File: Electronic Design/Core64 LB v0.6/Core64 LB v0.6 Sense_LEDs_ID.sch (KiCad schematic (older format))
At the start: 25 parts, among them J10 TSM-106-03-T-DV‎, J11 HEADER_8-PIN_0.1, J17 LED Cur. Mon., U1 74HC02, U3 LM393, U3 SN74LV1T125DBVR, U4 M24C02-RMN, U7 LM393

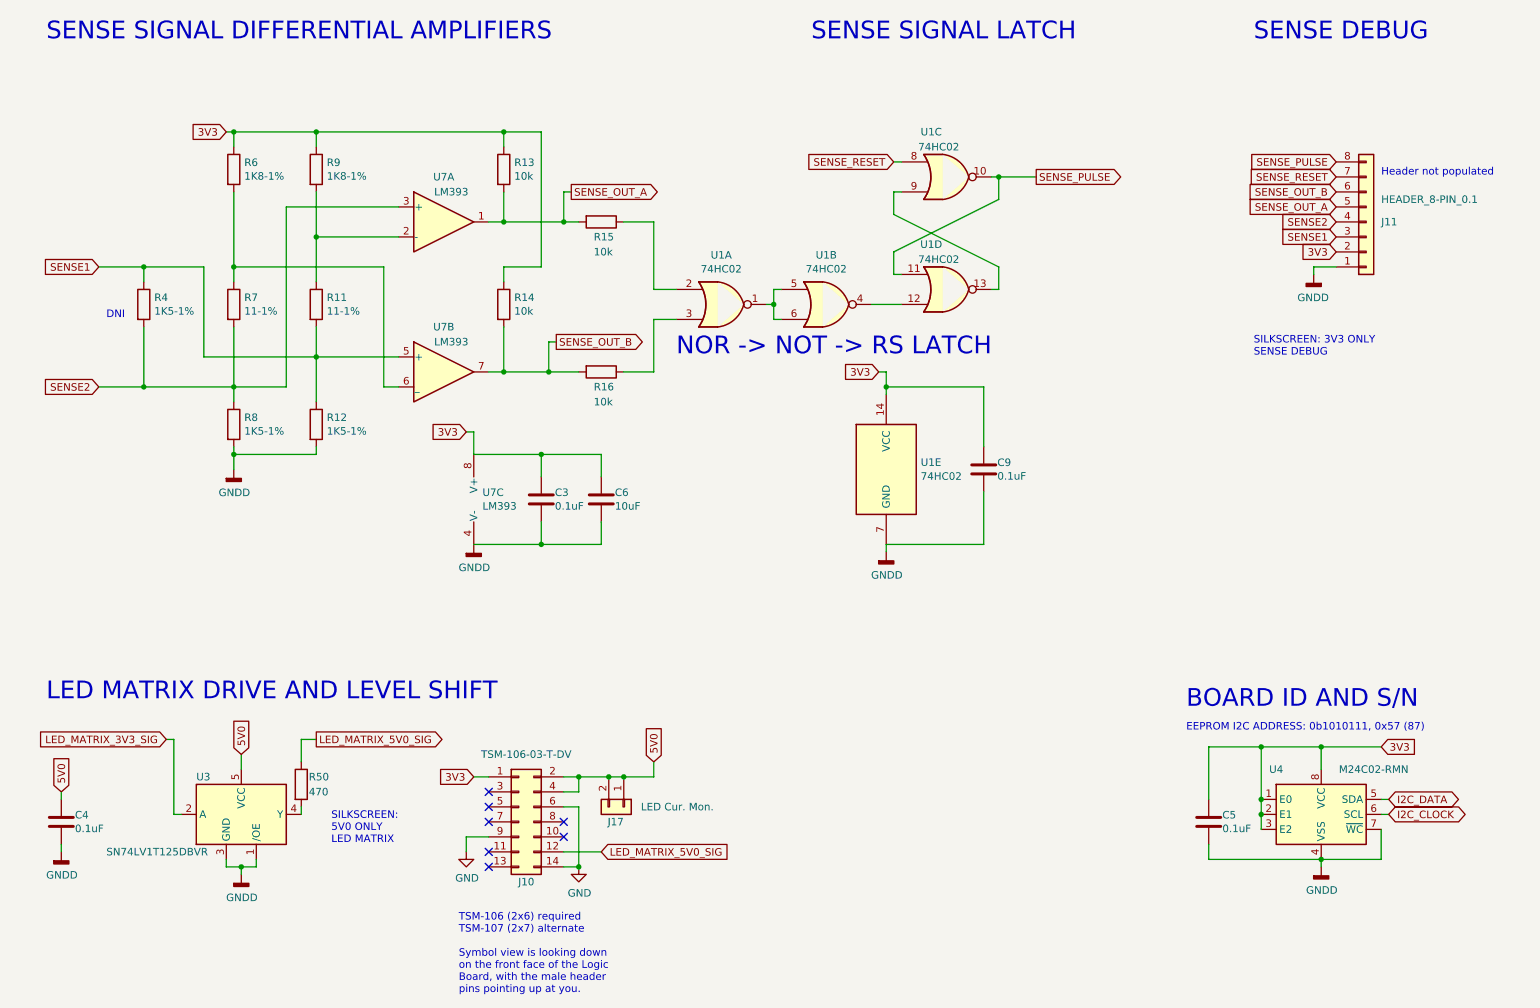
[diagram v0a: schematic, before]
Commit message: APPLY LOGIC BOARD V0.5 FIXES NEEDED TO BE V0.6 U1 silk screen should be placed by pin 1 not pin 7 Check J1 and J2 labels so J1 is on the left, like it is for the Core Board Remove Header for old LED Matrix, since is no longer needed and it is in the way. RTC Notes on schematic, must add THREE things, typo change from TWO. Below JP5 Teensy Charge Enable is a rogue "+" on the silk screen Left of R56 is a dead-end trace stub. Doesn't hurt anything but it's not right. 6.8 Ohm Core Current Limit Resistors can move to 5%. JP1/2 for OLED should be JP1/2 on the OLED silk screen, not JP3/4 Silk screen, left header row, swap SEN1 and SEN2 text so they match to S1 and S2 correctly on the inner perimeter. Move to larger logo and other text on the backside Update silk screen for all boards with P/Ns, bare board. Move top row of TFT LCD support down 0.55mm. Add 470 resistor to gate of core array enable to limit current. Change I2C pull-up resistors from 2.2K to 1.2K 20% (E12 series is most common, and values overlap) Remove two dead-end GND (BAT-) traces between/below Teensy 25/26, and over to QWIIC. Add I2C series resistors 68 Ohm at output of Teensy. Move the 470uF LED 5V0 capacitor, down to be between 5V0 Cur Mon and Teensy Charge enable jumpers, out of the way of the batteries. New stylus position is on left, so the 3V3 capacitor needs to move in a few mm to allow it to pass through. Provide thru-holes for alternate 3.3V and 5V bulk capacitor options. Propagation through sense logic chips was 200ns, reduce PU to 1K2 and remove inline 10Ks. Now 50ns. Voltage divider and other resistors, consolidated to 10K resistors. Keep the two 10K resistors on the 5V0 MON. Add a SJ in series to isolate from Hall Switches. Replace the inline 10K resistors in the all optional Voltage Monitoring lines with closed SJs instead. Clean-up all the horz/vert traces left from removing LED drive header and relocating the driver and 5V0 cap Part substitutions Data sheet updates
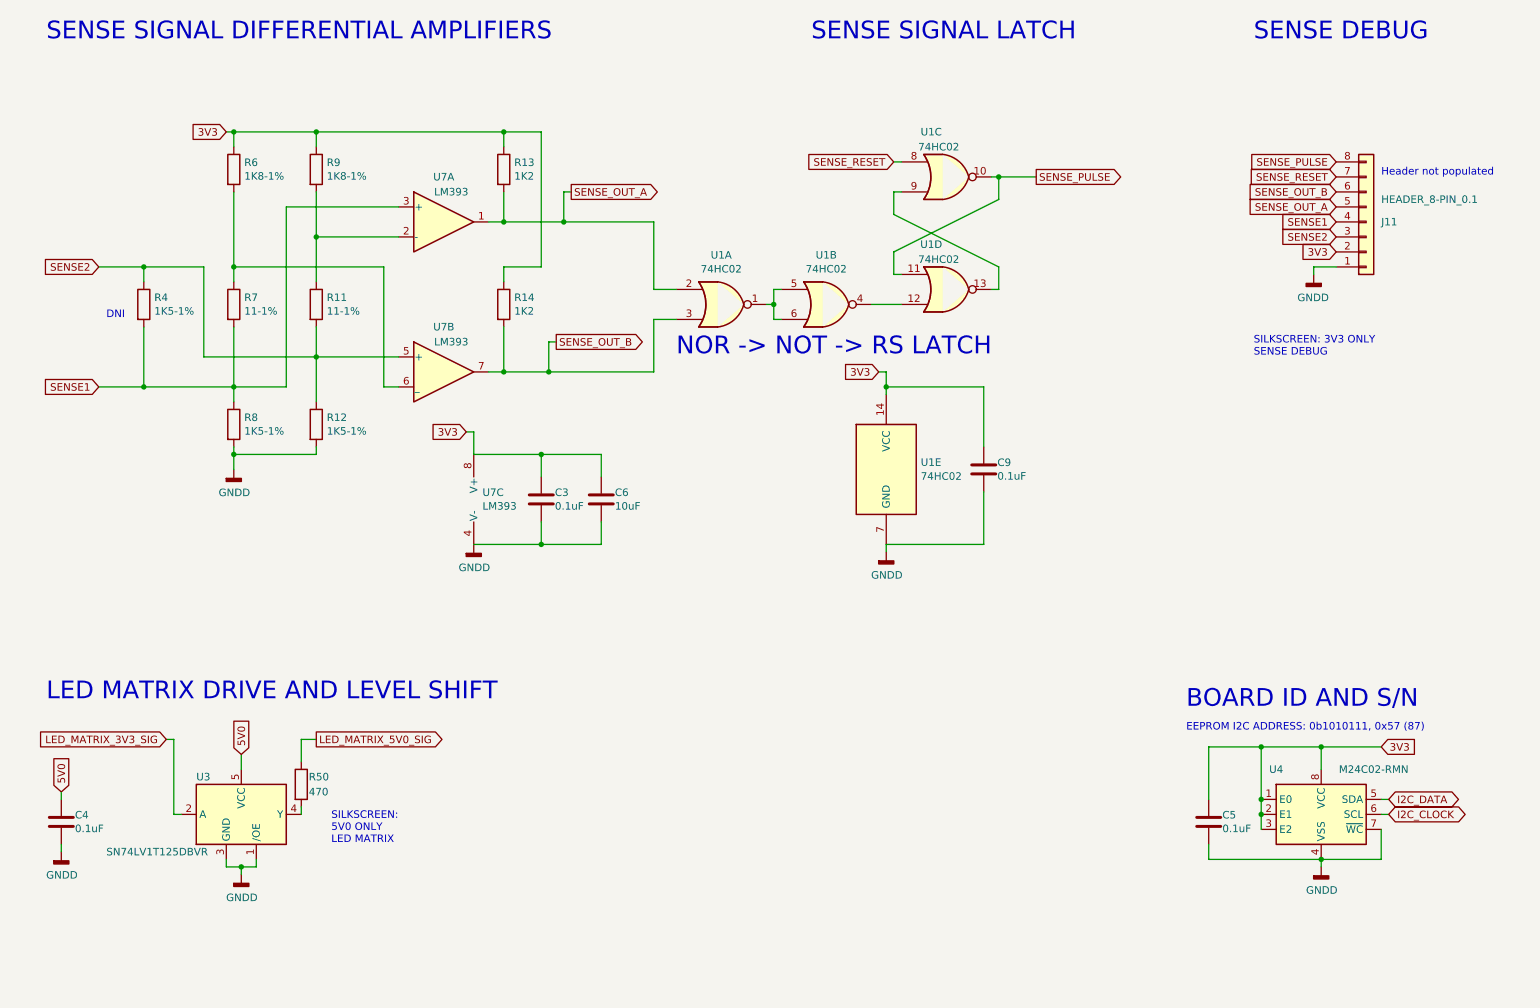
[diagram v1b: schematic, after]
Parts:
- removed J10: TSM-106-03-T-DV‎, Connector_PinHeader_2.54mm:PinHeader_2x07_P2.54mm_Vertical_SMD_and_TH, symbol Connector_Generic:Conn_02x07_Odd_Even
- removed J17: LED Cur. Mon., Connector_PinSocket_2.54mm:PinSocket_1x02_P2.54mm_Vertical, symbol Connector_Generic:Conn_01x02
- removed R15, R16: 10k, Resistor_SMD:R_0805_2012Metric, symbol Device:R
- R13, R14: value 10k -> 1K2
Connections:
- net SENSE1: now also J11.4 (Pin_4), R4.2, R7.2, R8.1, U3.3 (+); no longer J11.3 (Pin_3), R11.2, R12.1, R4.1, U7.5 (+)
- net SENSE2: now also J11.3 (Pin_3), R11.2, R12.1, R4.1, U7.5 (+); no longer J11.4 (Pin_4), R4.2, R7.2, R8.1, U3.3 (+)
- net SENSE_OUT_A: now also U1.2
- net SENSE_OUT_B: now also U1.3
- no-connect marks 7 -> 0
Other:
- note removed: "TSM-106 (2x6) required\nTSM-107 (2x7) alternate\n\nSymbol view is looking down\non the front face of the Logic\nBoard, with the male header\npins pointing up at you."
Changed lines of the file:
@@
 $EndComp
 Text GLabel 950  2350 0    50   Input ~ 0
+SENSE2
+Text GLabel 950  3150 0    50   Input ~ 0
 SENSE1
-Text GLabel 950  3150 0    50   Input ~ 0
-SENSE2
 $Comp
 L Device:R R6
@@
 P 3650 1700
 F 0 "R13" H 3720 1746 50  0000 L CNN
-F 1 "10k" H 3720 1655 50  0000 L CNN
+F 1 "1K2" H 3720 1655 50  0000 L CNN
 F 2 "Resistor_SMD:R_0805_2012Metric" V 3580 1700 50  0001 C CNN
 F 3 "~" H 3650 1700 50  0001 C CNN
@@
 P 3650 2600
 F 0 "R14" H 3720 2646 50  0000 L CNN
-F 1 "10k" H 3720 2555 50  0000 L CNN
+F 1 "1K2" H 3720 2555 50  0000 L CNN
 F 2 "Resistor_SMD:R_0805_2012Metric" V 3580 2600 50  0001 C CNN
 F 3 "~" H 3650 2600 50  0001 C CNN
@@
 Wire Wire Line
 	3650 2050 4050 2050
-$Comp
-L Device:R R16
-U 1 1 5E62BEBD
-P 4300 3050
-F 0 "R16" V 4400 3000 50  0000 L CNN
-F 1 "10k" V 4500 3000 50  0000 L CNN
-F 2 "Resistor_SMD:R_0805_2012Metric" V 4230 3050 50  0001 C CNN
-F 3 "~" H 4300 3050 50  0001 C CNN
-	1    4300 3050
-	0    1    1    0
-$EndComp
-$Comp
-L Device:R R15
-U 1 1 5E631504
-P 4300 2050
-F 0 "R15" V 4400 2000 50  0000 L CNN
-F 1 "10k" V 4500 2000 50  0000 L CNN
-F 2 "Resistor_SMD:R_0805_2012Metric" V 4230 2050 50  0001 C CNN
-F 3 "~" H 4300 2050 50  0001 C CNN
-	1    4300 2050
-	0    1    1    0
-$EndComp
 Wire Wire Line
 	4050 1850 4050 2050
 Connection ~ 4050 2050
 Wire Wire Line
-	4050 2050 4150 2050
-Wire Wire Line
 	3950 2850 3950 3050
 Connection ~ 3950 3050
-Wire Wire Line
-	3950 3050 4150 3050
 Wire Wire Line
 	2400 2950 2950 2950
@@
 	4650 2500 4800 2500
 Wire Wire Line
-	4450 2050 4650 2050
-Wire Wire Line
 	4800 2700 4650 2700
 Wire Wire Line
 	4650 2700 4650 3050
-Wire Wire Line
-	4450 3050 4650 3050
 Wire Wire Line
 	5400 2600 5450 2600
@@
 $EndComp
 Text GLabel 9200 2150 0    50   Input ~ 0
+SENSE2
+Text GLabel 9200 2050 0    50   Input ~ 0
 SENSE1
-Text GLabel 9200 2050 0    50   Input ~ 0
-SENSE2
 Wire Wire Line
 	1250 3150 1850 3150
@@
 Wire Wire Line
 	2300 5650 2300 5500
-NoConn ~ 3550 6350
-Text Notes 3350 7200 0    50   ~ 0
-TSM-106 (2x6) required\nTSM-107 (2x7) alternate\n\nSymbol view is looking down\non the front face of the Logic\nBoard, with the male header\npins pointing up at you.
 Text Notes 2500 6200 0    50   ~ 0
 SILKSCREEN: \n5V0 ONLY\nLED MATRIX
-Wire Wire Line
-	4650 5650 4650 5750
-Text GLabel 4650 5650 1    50   Input ~ 0
-5V0
-NoConn ~ 3550 5850
-NoConn ~ 3550 5950
-NoConn ~ 3550 6050
-NoConn ~ 3550 6250
-NoConn ~ 4050 6150
-NoConn ~ 4050 6050
-Wire Wire Line
-	3400 6150 3400 6250
-Wire Wire Line
-	3550 6150 3400 6150
-Wire Wire Line
-	4050 6250 4300 6250
-Wire Wire Line
-	4050 5750 4150 5750
-$Comp
-L power:GND #PWR?
-U 1 1 5F7F8247
-P 3400 6250
-AR Path="/5E755787/5F7F8247" Ref="#PWR?"  Part="1"
-AR Path="/5F7F8247" Ref="#PWR?"  Part="1"
-AR Path="/5E75D6AB/5F7F8247" Ref="#PWR0114"  Part="1"
-F 0 "#PWR0114" H 3400 6000 50  0001 C CNN
-F 1 "GND" H 3405 6075 50  0000 C CNN
-F 2 "" H 3400 6250 50  0001 C CNN
-F 3 "" H 3400 6250 50  0001 C CNN
-	1    3400 6250
-	1    0    0    -1
-$EndComp
-Text GLabel 4300 6250 2    50   Input ~ 0
-LED_MATRIX_5V0_SIG
-$Comp
-L Connector_Generic:Conn_02x07_Odd_Even J?
-U 1 1 5F7F824E
-P 3750 6050
-AR Path="/5F7F824E" Ref="J?"  Part="1"
-AR Path="/5E75D6AB/5F7F824E" Ref="J10"  Part="1"
-F 0 "J10" H 3800 5650 50  0000 C CNN
-F 1 "TSM-106-03-T-DV‎" H 3800 6500 50  0000 C CNN
-F 2 "Connector_PinHeader_2.54mm:PinHeader_2x07_P2.54mm_Vertical_SMD_and_TH" H 3750 6050 50  0001 C CNN
-F 3 "~" H 3750 6050 50  0001 C CNN
-	1    3750 6050
-	1    0    0    -1
-$EndComp
 $Comp
 L Logic_LevelTranslator:SN74LV1T125DBVR U?
@@
 	1    0    0    -1
 $EndComp
-$Comp
-L Connector_Generic:Conn_01x02 J?
-U 1 1 5F951C5C
-P 4450 5950
-AR Path="/5E7548ED/5F951C5C" Ref="J?"  Part="1"
-AR Path="/5E75D6AB/5F951C5C" Ref="J17"  Part="1"
-F 0 "J17" V 4550 5950 50  0000 R CNN
-F 1 "LED Cur. Mon." V 4450 6550 50  0000 R CNN
-F 2 "Connector_PinSocket_2.54mm:PinSocket_1x02_P2.54mm_Vertical" H 4450 5950 50  0001 C CNN
-F 3 "~" H 4450 5950 50  0001 C CNN
-	1    4450 5950
-	0    1    1    0
-$EndComp
-Wire Wire Line
-	4450 5750 4350 5750
-Connection ~ 4450 5750
-Wire Wire Line
-	4450 5750 4650 5750
-Connection ~ 4350 5750
-Text GLabel 3450 5750 0    50   Input ~ 0
-3V3
-Wire Wire Line
-	3450 5750 3550 5750
-Wire Wire Line
-	4050 5850 4150 5850
-Wire Wire Line
-	4150 5850 4150 5750
-Connection ~ 4150 5750
-Wire Wire Line
-	4150 5750 4350 5750
-Wire Wire Line
-	4050 5950 4150 5950
-Wire Wire Line
-	4150 5950 4150 6350
-Wire Wire Line
-	4150 6350 4050 6350
-$Comp
-L power:GND #PWR?
-U 1 1 5FB058FB
-P 4150 6350
-AR Path="/5E755787/5FB058FB" Ref="#PWR?"  Part="1"
-AR Path="/5FB058FB" Ref="#PWR?"  Part="1"
-AR Path="/5E75D6AB/5FB058FB" Ref="#PWR0107"  Part="1"
-F 0 "#PWR0107" H 4150 6100 50  0001 C CNN
-F 1 "GND" H 4155 6175 50  0000 C CNN
-F 2 "" H 4150 6350 50  0001 C CNN
-F 3 "" H 4150 6350 50  0001 C CNN
-	1    4150 6350
-	1    0    0    -1
-$EndComp
-Connection ~ 4150 6350
 Wire Wire Line
 	9500 5900 9550 5900
 Wire Wire Line
 	9500 6000 9550 6000
+Wire Wire Line
+	4050 2050 4650 2050
+Wire Wire Line
+	3950 3050 4650 3050
 $EndSCHEMATC

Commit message: Revise LB V0.6, part substitutions, data sheet updates, clean up Ref. Des. to be in order and easier to find on the board in groups
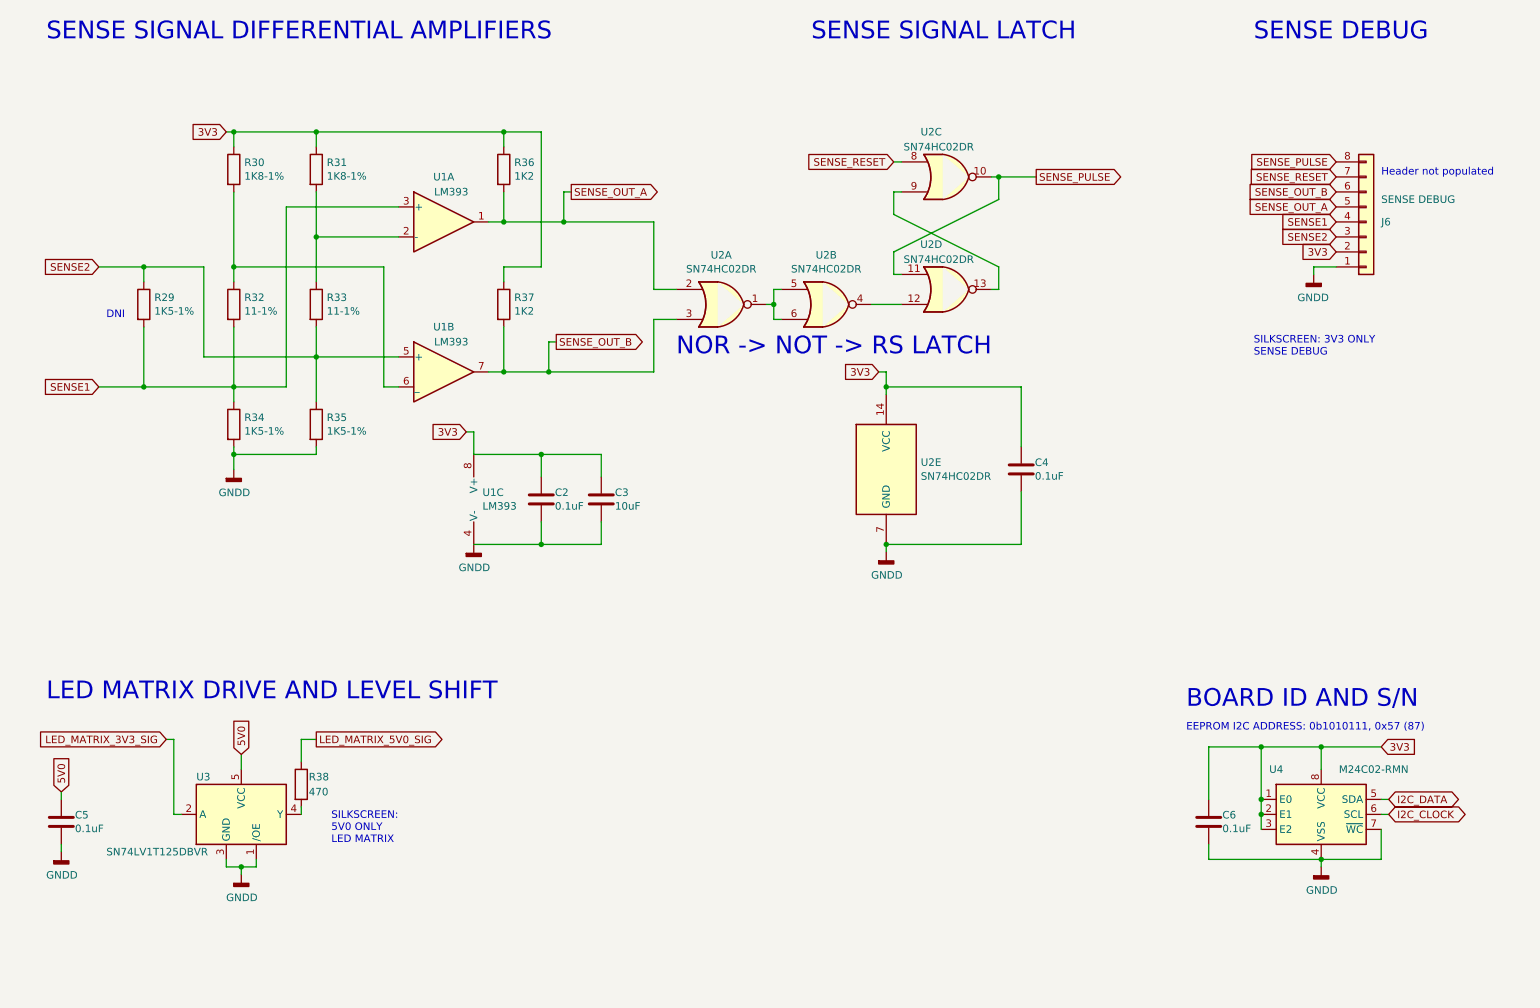
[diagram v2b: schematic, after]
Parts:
- C2: renamed from C3; Description (none) -> CAP; Insert? (none) -> Yes
- C3: renamed from C6; Description (none) -> CAP; Insert? (none) -> Yes
- C4: renamed from C9; Description (none) -> CAP; Insert? (none) -> Yes
- C5: renamed from C4; Description (none) -> CAP; Insert? (none) -> Yes
- C6: renamed from C5; Description (none) -> CAP; Insert? (none) -> Yes
- J6: renamed from J11; value HEADER_8-PIN_0.1 -> SENSE DEBUG; Insert? (none) -> No
- R29: renamed from R4; Description (none) -> RES 1.5K OHM; Insert? (none) -> Yes; Value_Modifier (none) -> 1%
- R30: renamed from R6; Description (none) -> RES 1.8K OHM; Insert? (none) -> Yes; Value_Modifier (none) -> 1%
- R31: renamed from R9; Description (none) -> RES 1.8K OHM; Insert? (none) -> Yes; Value_Modifier (none) -> 1%
- R32: renamed from R7; Description (none) -> RES 1 OHM; Insert? (none) -> Yes; Value_Modifier (none) -> 1%
- R33: renamed from R11; Description (none) -> RES 1 OHM; Insert? (none) -> Yes; Value_Modifier (none) -> 1%
- R34: renamed from R8; Description (none) -> RES 1.5K OHM; Insert? (none) -> Yes; Value_Modifier (none) -> 1%
- R35: renamed from R12; Description (none) -> RES 1.5K OHM; Insert? (none) -> Yes; Value_Modifier (none) -> 1%
- R36: renamed from R13; Description (none) -> RES 1.2K OHM; Insert? (none) -> Yes; Value_Modifier (none) -> 10%
- R37: renamed from R14; Description (none) -> RES 1.2K OHM; Insert? (none) -> Yes; Value_Modifier (none) -> 10%
- R38: renamed from R50; Description (none) -> RES 470 OHM; Insert? (none) -> Yes; Value_Modifier (none) -> 10%
- U1: renamed from U7; Description (none) -> IC COMPARATOR LP DUAL 8-SOIC; Insert? (none) -> Yes; MPN (none) -> LM393DT; MPN(Secondary) (none) -> LM393DR; Manufacturer(Secondary) (none) -> Rohm; Manufacturer_Name (none) -> STMicroelectronics
- U2: renamed from U1; value 74HC02 -> SN74HC02DR; Description (none) -> IC GATE NOR 4CH 2-INP 14SOIC; Insert? (none) -> Yes; MPN (none) -> SN74HC02DR; Manufacturer_Name (none) -> Texas Instruments
- U3: Description (none) -> IC COMPARATOR LP DUAL 8-SOIC; Insert? (none) -> Yes; MPN (none) -> LM393DT; MPN(Secondary) (none) -> LM393DR; Manufacturer(Secondary) (none) -> Rohm; Manufacturer_Name (none) -> STMicroelectronics
- U3: Description (none) -> IC BUF NON-INVERT 5.5V SOT23-5; Insert? (none) -> Yes; MPN (none) -> SN74LV1T125DBVR; MPN(Secondary) (none) -> M74VHC1GT125DT1G; Manufacturer(Secondary) (none) -> OnSemi; Manufacturer_Name (none) -> Texas Instruments
- U4: Description (none) -> IC EEPROM 2KBIT I2C 400KHZ 8SO; Insert? (none) -> Yes; MPN (none) -> M24C02-WMN6TP; Manufacturer_Name (none) -> STMicroelectronics
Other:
- moved on the sheet: C4

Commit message: Refine LB v0.6 layout, KiCAD BOM updates, review schematic and PCB for release
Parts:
- R29: Insert? Yes -> No
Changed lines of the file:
@@
 Sheet 2 5
 Title "Core 64 - Sense"
-Date "2021-11-08"
+Date "2021-11-09"
 Rev "0.6"
 Comp "Concept and design by Andy Geppert @ www.MachineIdeas.com"
 Comment1 "Visit www.Core64.io for information on assembly and optional features."
-Comment2 "WIP"
+Comment2 "As released"
 Comment3 ""
 Comment4 "All non-polarized capacitors are X7R or X5R ceramic unless otherwise noted."
@@
 F 4 "RES 1.5K OHM" H 1250 2600 50  0001 C CNN "Description"
 F 5 "1%" H 1250 2600 50  0001 C CNN "Value_Modifier"
-F 6 "Yes" H 1250 2600 50  0001 C CNN "Insert?"
+F 6 "No" H 1250 2600 50  0001 C CNN "Insert?"
 	1    1250 2600
 	1    0    0    -1
